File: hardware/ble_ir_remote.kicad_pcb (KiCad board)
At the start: 2 copper layers, 40.1 x 40 mm, 29 parts, among them Q1 MMBT3904, U1 ESP32-C3-MINI-1-N4

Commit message: sch progress
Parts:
- added U2: XC6206PxxxMR, Package_TO_SOT_SMD:SOT-23, F.Cu at (138.4, 122.9)
- S1: value TS-1187A-B -> STANDBY
- S2: value TS-1187A-B -> RESET
- S3: value TS-1187A-B -> VOLUME+
- S4: value TS-1187A-B -> VOLUME-
- S5: value TS-1187A-B -> BASS+
- S6: value TS-1187A-B -> BASS-
- S7: value TS-1187A-B -> PROG-1
- S8: value TS-1187A-B -> PROG2
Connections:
- C1 pad 1: /SW1 -> /SW_STANDBY
- C2 pad 1: /SW2 -> /SW_RESET
- C3 pad 1: /SW3 -> /SW_VOLP
- C4 pad 1: /SW4 -> /SW_VOLM
- C5 pad 1: /SW5 -> /SW_BASSP
- C6 pad 1: /SW6 -> /SW_BASSM
- C7 pad 1: /SW7 -> /SW_PROG1
- C8 pad 1: /SW8 -> /SW_PROG2
- R10 pad 2: /SW8 -> /SW_PROG2
- R3 pad 2: /SW1 -> /SW_STANDBY
- R4 pad 2: /SW2 -> /SW_RESET
- R5 pad 2: /SW3 -> /SW_VOLP
- R6 pad 2: /SW4 -> /SW_VOLM
- R7 pad 2: /SW5 -> /SW_BASSP
- R8 pad 2: /SW6 -> /SW_BASSM
- R9 pad 2: /SW7 -> /SW_PROG1
- U1 pad 12: unconnected-(U1-Pad12) -> /SW_STANDBY
- U1 pad 13: unconnected-(U1-Pad13) -> /SW_RESET
- U1 pad 16: unconnected-(U1-Pad16) -> /SW_PROG2
- U1 pad 18: unconnected-(U1-Pad18) -> /SW_BASSP
- U1 pad 19: unconnected-(U1-Pad19) -> /SW_BASSM
- U1 pad 20: unconnected-(U1-Pad20) -> /SW_PROG1
- U1 pad 5: unconnected-(U1-Pad5) -> /SW_VOLP
- U1 pad 6: unconnected-(U1-Pad6) -> /SW_VOLM

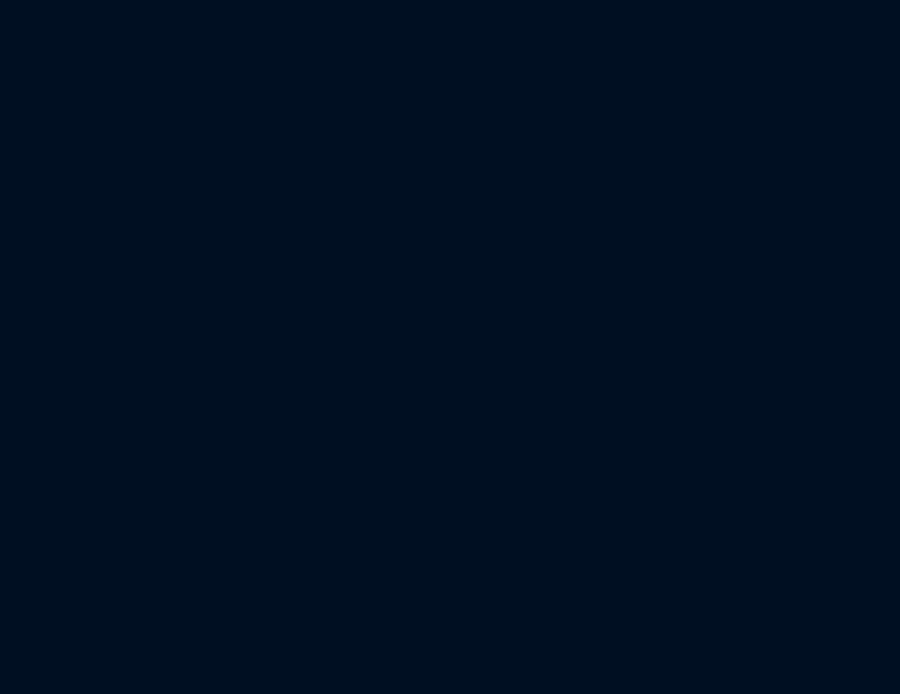
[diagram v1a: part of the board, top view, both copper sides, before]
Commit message: usb conn added
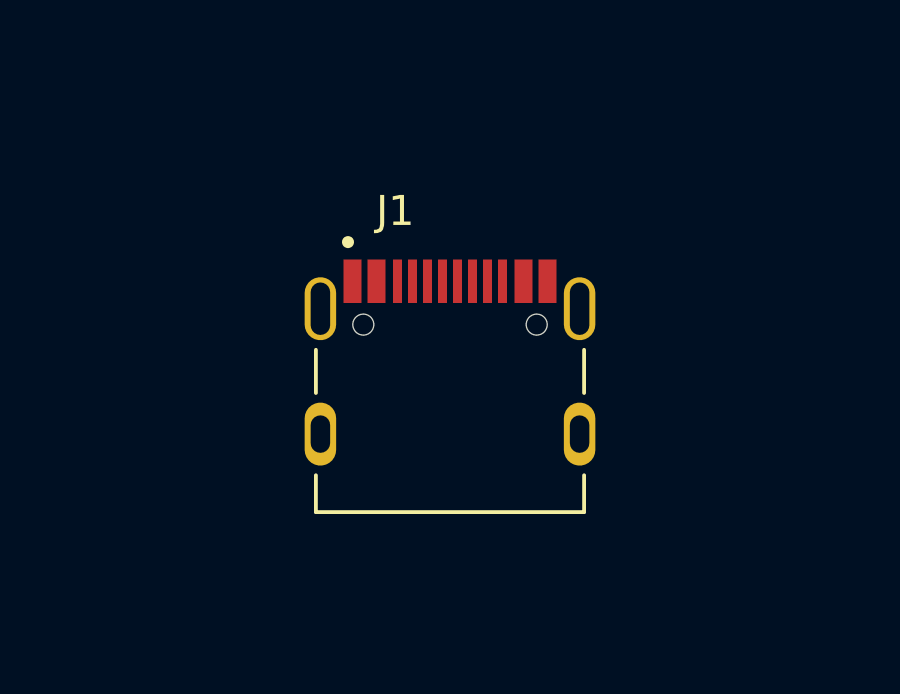
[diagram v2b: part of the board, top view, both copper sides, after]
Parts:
- added J1: TYPE-C-31-M-12, TYPE-C-31-M-12:HRO_TYPE-C-31-M-12, F.Cu at (106.7, 114.3)
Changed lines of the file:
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@@
   (net 43 "Net-(R9-Pad1)")
   (net 44 "Net-(R10-Pad1)")
+  (net 45 "unconnected-(J1-PadA6)")
+  (net 46 "unconnected-(J1-PadB7)")
+  (net 47 "unconnected-(J1-PadA5)")
+  (net 48 "unconnected-(J1-PadB8)")
+  (net 49 "unconnected-(J1-PadA7)")
+  (net 50 "unconnected-(J1-PadB6)")
+  (net 51 "unconnected-(J1-PadA8)")
+  (net 52 "unconnected-(J1-PadB5)")
+  (net 53 "Net-(J1-PadS1)")
   (footprint "Capacitor_SMD:C_0603_1608Metric" (layer "F.Cu")
     (at 99.05 92.175)
@@
       (offset (xyz 0 0 0))
       (scale (xyz 1 1 1))
+      (rotate (xyz -90 0 0))
+    )
+  )
+  (footprint "TYPE-C-31-M-12:HRO_TYPE-C-31-M-12" (layer "F.Cu")
+    (at 106.68 114.3)
+    (property "MANUFACTURER" "HRO Electronics")
+    (property "MAXIMUM_PACKAGE_HEIGHT" "3.31mm")
+    (property "PARTREV" "A")
+    (property "STANDARD" "Manufacturer Recommendations")
+    (property "Sheetfile" "ble_ir_remote.kicad_sch")
+    (property "Sheetname" "")
+    (attr through_hole)
+    (fp_text reference "J1" (at -1.825 -7.435) (layer "F.SilkS")
+      (effects (font (size 1 1) (thickness 0.15)))
+    )
+    (fp_text value "TYPE-C-31-M-12" (at 6.43 4.135) (layer "F.Fab")
+      (effects (font (size 1 1) (thickness 0.15)))
+    )
+    (fp_line (start -4.47 2.6) (end -4.47 1.37) (layer "F.SilkS") (width 0.127))
+    (fp_line (start 4.47 1.37) (end 4.47 2.6) (layer "F.SilkS") (width 0.127))
+    (fp_line (start 4.47 2.6) (end -4.47 2.6) (layer "F.SilkS") (width 0.127))
+    (fp_line (start -4.47 -2.81) (end -4.47 -1.37) (layer "F.SilkS") (width 0.127))
+    (fp_line (start 4.47 -2.81) (end 4.47 -1.37) (layer "F.SilkS") (width 0.127))
+    (fp_circle (center -3.4 -6.4) (end -3.3 -6.4) (layer "F.SilkS") (width 0.2) (fill none))
+    (fp_line (start -5.095 2.85) (end 5.095 2.85) (layer "F.CrtYd") (width 0.05))
+    (fp_line (start 5.095 -6.07) (end -5.095 -6.07) (layer "F.CrtYd") (width 0.05))
+    (fp_line (start -5.095 -6.07) (end -5.095 2.85) (layer "F.CrtYd") (width 0.05))
+    (fp_line (start 5.095 2.85) (end 5.095 -6.07) (layer "F.CrtYd") (width 0.05))
+    (fp_line (start -4.47 2.6) (end 4.47 2.6) (layer "F.Fab") (width 0.127))
+    (fp_line (start 4.47 -4.7) (end -4.47 -4.7) (layer "F.Fab") (width 0.127))
+    (fp_line (start 4.47 2.6) (end 4.47 -4.7) (layer "F.Fab") (width 0.127))
+    (fp_line (start -4.47 -4.7) (end -4.47 2.6) (layer "F.Fab") (width 0.127))
+    (fp_circle (center -3.4 -6.4) (end -3.3 -6.4) (layer "F.Fab") (width 0.2) (fill none))
+    (pad "" np_thru_hole circle locked (at 2.89 -3.65) (size 0.7 0.7) (drill 0.7) (layers *.Cu *.Mask))
+    (pad "" np_thru_hole circle locked (at -2.89 -3.65) (size 0.7 0.7) (drill 0.7) (layers *.Cu *.Mask))
+    (pad "A1B12" smd rect locked (at -3.25 -5.095) (size 0.6 1.45) (layers "F.Cu" "F.Paste" "F.Mask")
+      (net 18 "GND") (pinfunction "GND") (pintype "power_in"))
+    (pad "A4B9" smd rect locked (at -2.45 -5.095) (size 0.6 1.45) (layers "F.Cu" "F.Paste" "F.Mask")
+      (net 35 "VBUS") (pinfunction "VBUS") (pintype "power_in"))
+    (pad "A5" smd rect locked (at -1.25 -5.095) (size 0.3 1.45) (layers "F.Cu" "F.Paste" "F.Mask")
+      (net 47 "unconnected-(J1-PadA5)") (pinfunction "CC1") (pintype "bidirectional"))
+    (pad "A6" smd rect locked (at -0.25 -5.095) (size 0.3 1.45) (layers "F.Cu" "F.Paste" "F.Mask")
+      (net 45 "unconnected-(J1-PadA6)") (pinfunction "DP1") (pintype "bidirectional"))
+    (pad "A7" smd rect locked (at 0.25 -5.095) (size 0.3 1.45) (layers "F.Cu" "F.Paste" "F.Mask")
+      (net 49 "unconnected-(J1-PadA7)") (pinfunction "DN1") (pintype "bidirectional"))
+    (pad "A8" smd rect locked (at 1.25 -5.095) (size 0.3 1.45) (layers "F.Cu" "F.Paste" "F.Mask")
+      (net 51 "unconnected-(J1-PadA8)") (pinfunction "SBU1") (pintype "bidirectional"))
+    (pad "B1A12" smd rect locked (at 3.25 -5.095) (size 0.6 1.45) (layers "F.Cu" "F.Paste" "F.Mask")
+      (net 18 "GND") (pinfunction "GND") (pintype "power_in"))
+    (pad "B4A9" smd rect locked (at 2.45 -5.095) (size 0.6 1.45) (layers "F.Cu" "F.Paste" "F.Mask")
+      (net 35 "VBUS") (pinfunction "VBUS") (pintype "power_in"))
+    (pad "B5" smd rect locked (at 1.75 -5.095) (size 0.3 1.45) (layers "F.Cu" "F.Paste" "F.Mask")
+      (net 52 "unconnected-(J1-PadB5)") (pinfunction "CC2") (pintype "bidirectional"))
+    (pad "B6" smd rect locked (at 0.75 -5.095) (size 0.3 1.45) (layers "F.Cu" "F.Paste" "F.Mask")
+      (net 50 "unconnected-(J1-PadB6)") (pinfunction "DP2") (pintype "bidirectional"))
+    (pad "B7" smd rect locked (at -0.75 -5.095) (size 0.3 1.45) (layers "F.Cu" "F.Paste" "F.Mask")
+      (net 46 "unconnected-(J1-PadB7)") (pinfunction "DN2") (pintype "bidirectional"))
+    (pad "B8" smd rect locked (at -1.75 -5.095) (size 0.3 1.45) (layers "F.Cu" "F.Paste" "F.Mask")
+      (net 48 "unconnected-(J1-PadB8)") (pinfunction "SBU2") (pintype "bidirectional"))
+    (pad "S1" thru_hole oval locked (at -4.32 -4.18) (size 1.05 2.1) (drill oval 0.65 1.75) (layers *.Cu *.Mask)
+      (net 53 "Net-(J1-PadS1)") (pinfunction "SHIELD") (pintype "passive"))
+    (pad "S2" thru_hole oval locked (at 4.32 -4.18) (size 1.05 2.1) (drill oval 0.65 1.75) (layers *.Cu *.Mask)
+      (net 53 "Net-(J1-PadS1)") (pinfunction "SHIELD") (pintype "passive"))
+    (pad "S3" thru_hole oval locked (at -4.32 0) (size 1.05 2.1) (drill oval 0.65 1.25) (layers *.Cu *.Mask)
+      (net 53 "Net-(J1-PadS1)") (pinfunction "SHIELD") (pintype "passive"))
+    (pad "S4" thru_hole oval locked (at 4.32 0) (size 1.05 2.1) (drill oval 0.65 1.25) (layers *.Cu *.Mask)
+      (net 53 "Net-(J1-PadS1)") (pinfunction "SHIELD") (pintype "passive"))
+    (model "${KIPRJMOD}/lib/TYPE-C-31-M-12/TYPE-C-31-M-12.step"
+      (offset (xyz 0 0 0))
+      (scale (xyz 1 1 1))

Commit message: sch prgs
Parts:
- added C10: 100n, Capacitor_SMD:C_0603_1608Metric, F.Cu at (117.3, 125.3)
- added C11: 100n, Capacitor_SMD:C_0603_1608Metric, F.Cu at (109.3, 127.2)
- added C12: 100n, Capacitor_SMD:C_0603_1608Metric, F.Cu at (110.5, 122.7)
- added C9: 100n, Capacitor_SMD:C_0603_1608Metric, F.Cu at (117.3, 127.8)
- added D2: Heartbeat, LED_SMD:LED_0603_1608Metric, F.Cu at (126.2, 116.6)
- added J2: Debug connector, Connector_PinHeader_2.54mm:PinHeader_1x08_P2.54mm_Vertical, F.Cu at (126.5, 95.2)
- added R11: 5.1K, Resistor_SMD:R_0603_1608Metric, F.Cu at (113.3, 125.3)
- added R12: 5.1K, Resistor_SMD:R_0603_1608Metric, F.Cu at (114.5, 122.7)
- added R13: 120R, Resistor_SMD:R_0603_1608Metric, F.Cu at (105.3, 127.2)
- added R14: 10K, Resistor_SMD:R_0603_1608Metric, F.Cu at (113.3, 127.8)
- added U3: SRV05-4, Package_TO_SOT_SMD:SOT-23-6, F.Cu at (105.9, 123.7)
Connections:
- J1 pad A5: unconnected-(J1-PadA5) -> Net-(J1-PadA5)
- J1 pad A6: unconnected-(J1-PadA6) -> /USB_D+
- J1 pad A7: unconnected-(J1-PadA7) -> /USB_D-
- J1 pad B5: unconnected-(J1-PadB5) -> Net-(J1-PadB5)
- J1 pad B6: unconnected-(J1-PadB6) -> /USB_D+
- J1 pad B7: unconnected-(J1-PadB7) -> /USB_D-
- U1 pad 22: unconnected-(U1-Pad22) -> /BOOT1
- U1 pad 26: unconnected-(U1-Pad26) -> /USB_D-
- U1 pad 27: unconnected-(U1-Pad27) -> /USB_D+
- U1 pad 30: unconnected-(U1-Pad30) -> /RXD0
- U1 pad 31: unconnected-(U1-Pad31) -> /TXD0
